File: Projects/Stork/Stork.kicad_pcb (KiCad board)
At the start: 4 copper layers, 200 x 100 mm, 567 parts, among them J1 Conn_01x05, J10 Conn_01x05, J11 Conn_01x05, J12 Conn_01x05, J13 Conn_01x05, J14 Conn_01x05, J15 Conn_01x05, J16 Conn_01x05, J17 Conn_01x05, J18 Conn_01x05, J19 Conn_01x05, J2 Conn_01x05, J20 Conn_01x05, J21 Conn_01x05, J22 Conn_01x05, J23 Conn_01x05, J24 Conn_01x05, J25 Conn_02x03_Odd_Even, J26 Conn_01x03_Male, J27 Screw_Terminal_01x02, J28 Conn_01x03_Male, J29 Conn_01x03_Male, J3 Conn_01x05, J30 Conn_01x03_Male, J4 Conn_01x05, J5 Conn_01x05, J6 Conn_01x05, J7 Conn_01x05, J8 Conn_01x05, J9 Conn_01x05, U1 AD7991YRJZ-1500RL7, U10 AD8608ARZ-SOIC127P600X175-14N, U11 AD7991YRJZ-1500RL7, U12 AD8608ARZ-SOIC127P600X175-14N, U13 AD7991YRJZ-1500RL7, U14 AD8608ARZ-SOIC127P600X175-14N, U15 AD7991YRJZ-1500RL7, U16 AD8608ARZ-SOIC127P600X175-14N, U17 AD7991YRJZ-1500RL7, U18 AD8608ARZ-SOIC127P600X175-14N, U19 AD7991YRJZ-1500RL7, U2 AD8608ARZ-SOIC127P600X175-14N, U20 AD8608ARZ-SOIC127P600X175-14N, U21 AD7991YRJZ-1500RL7, U22 AD8608ARZ-SOIC127P600X175-14N, U23 AD7991YRJZ-1500RL7, U24 AD8608ARZ-SOIC127P600X175-14N, U25 AD7991YRJZ-1500RL7, U26 AD8608ARZ-SOIC127P600X175-14N, U27 AD7991YRJZ-1500RL7, U28 AD8608ARZ-SOIC127P600X175-14N, U29 AD7991YRJZ-1500RL7, U3 AD7991YRJZ-1500RL7, U30 AD8608ARZ-SOIC127P600X175-14N, U31 AD7991YRJZ-1500RL7, U32 AD8608ARZ-SOIC127P600X175-14N, U33 Digilent-CoraZ7, U34 AD7991YRJZ-1500RL7, U35 AD8608ARZ-SOIC127P600X175-14N, U36 AD7991YRJZ-1500RL7, U37 AD8608ARZ-SOIC127P600X175-14N, U38 AD7991YRJZ-1500RL7, U39 AD8608ARZ-SOIC127P600X175-14N, U4 AD8608ARZ-SOIC127P600X175-14N, U40 AD7991YRJZ-1500RL7, U41 AD8608ARZ-SOIC127P600X175-14N, U42 AD7991YRJZ-1500RL7, U43 AD8608ARZ-SOIC127P600X175-14N, U44 AD7991YRJZ-1500RL7, U45 AD8608ARZ-SOIC127P600X175-14N, U46 AD7991YRJZ-1500RL7, U47 AD8608ARZ-SOIC127P600X175-14N, U48 AD7991YRJZ-1500RL7, U49 AD8608ARZ-SOIC127P600X175-14N, U5 AD7991YRJZ-1500RL7, U50 TPS79330-EP, U51 TPS73150DBV, U6 AD8608ARZ-SOIC127P600X175-14N, U7 AD7991YRJZ-1500RL7, U8 AD8608ARZ-SOIC127P600X175-14N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

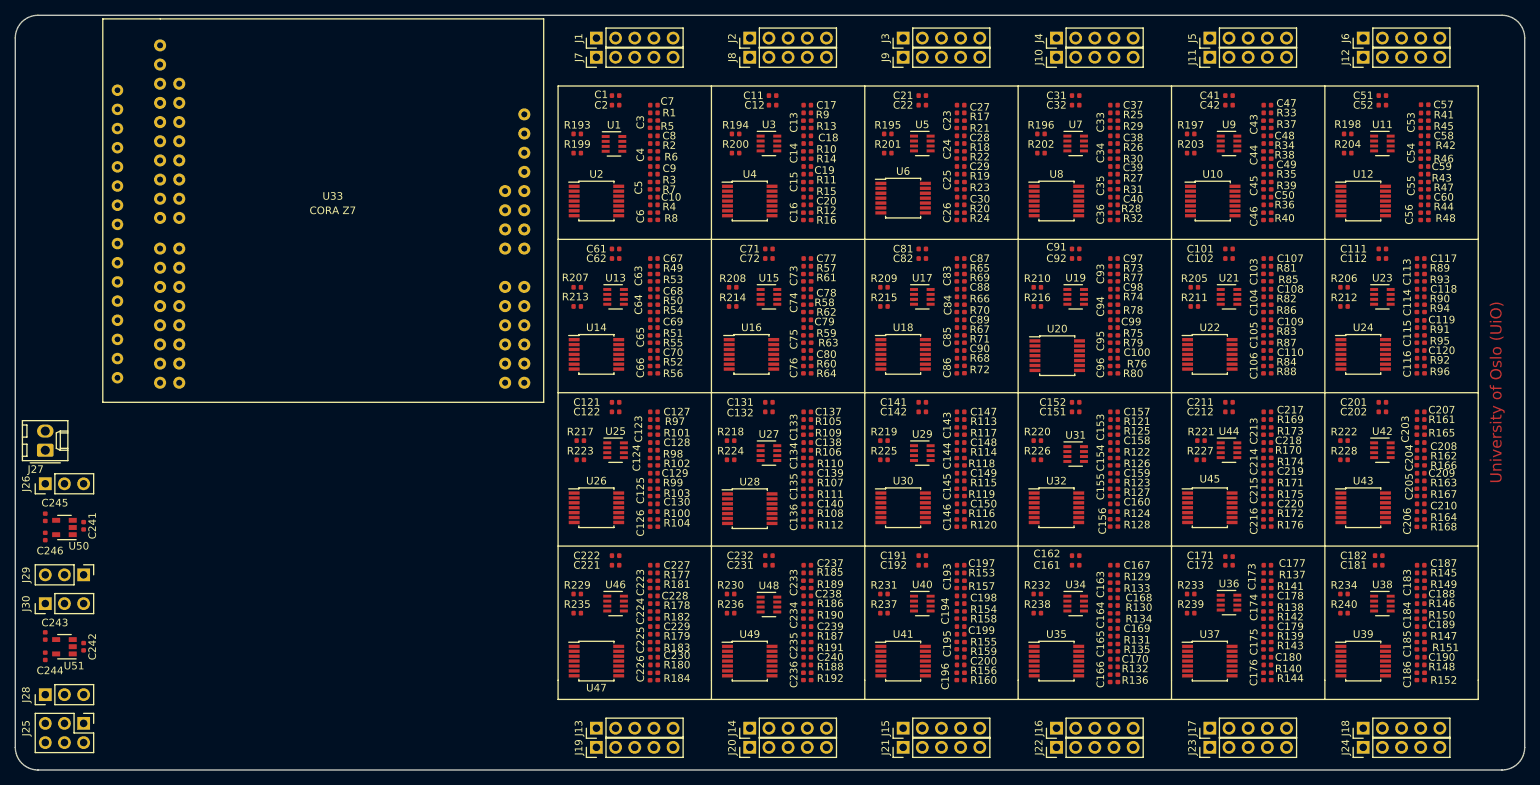
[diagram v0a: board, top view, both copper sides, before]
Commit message: replaced position of decoupling capacitors
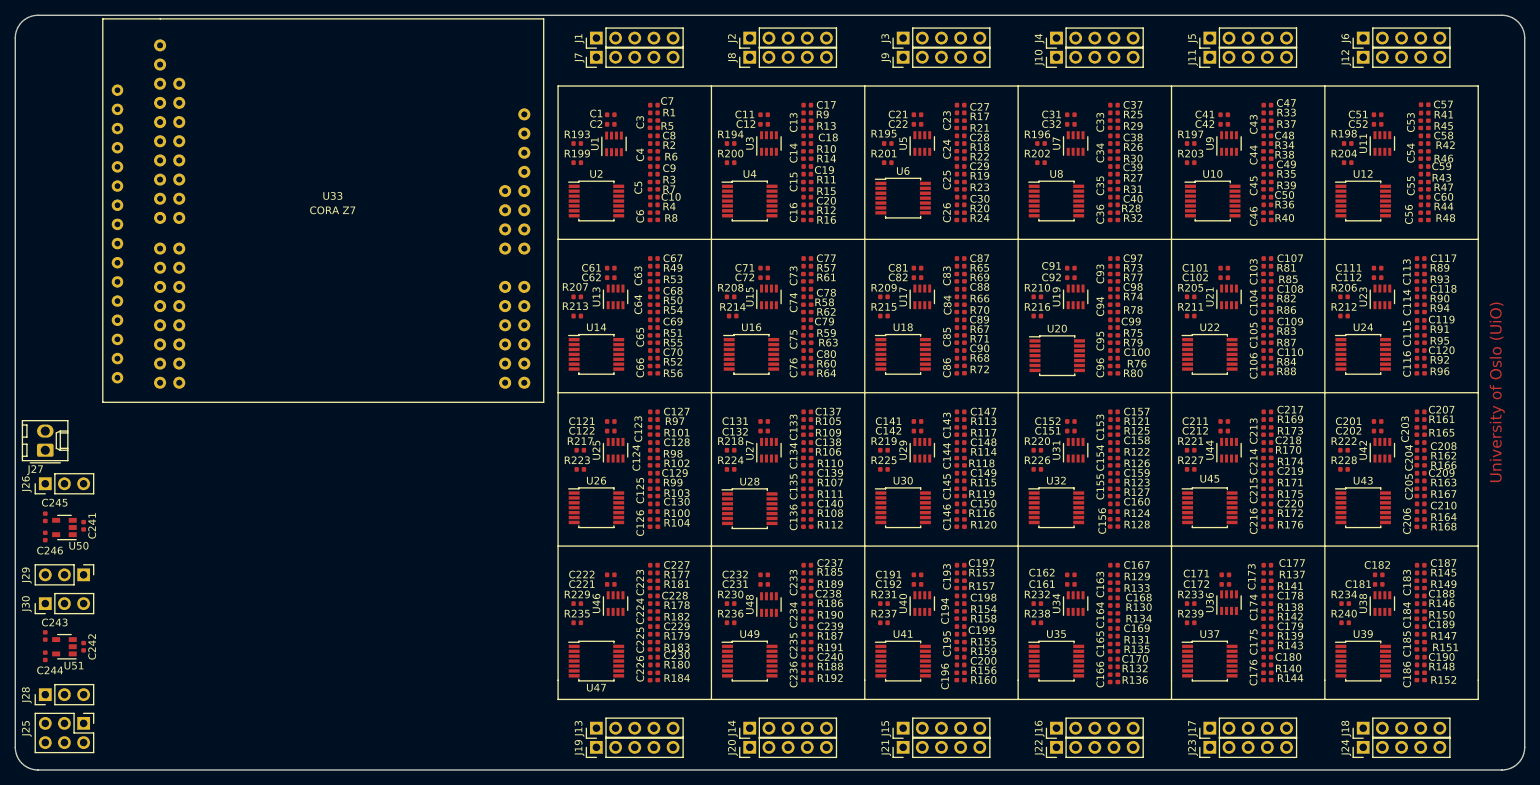
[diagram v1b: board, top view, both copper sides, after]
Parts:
- moved C12 2.78 mm to (149.2, 44.5)
- moved C11 2.78 mm to (149.2, 43.2)
- moved C132 2.62 mm to (149.2, 85.1)
- moved C142 2.62 mm to (169.5, 85.1)
- moved C191 2.62 mm to (169.5, 104.1)
- moved C22 2.62 mm to (169.5, 44.5)
- moved C232 2.62 mm to (149.2, 104.1)
- moved C122 2.62 mm to (128.9, 85.1)
- moved C151 2.62 mm to (189.9, 85.1)
- moved C162 2.62 mm to (189.9, 104.1)
- moved C2 2.62 mm to (128.9, 44.5)
- moved C202 2.62 mm to (230.5, 85.1)
- moved C212 2.62 mm to (210.2, 85.1)
- moved C222 2.62 mm to (128.9, 104.1)
- moved C32 2.62 mm to (189.9, 44.5)
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
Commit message: added vias for direct connection to ground and 3.3V plane. Done routing for power section
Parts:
- moved U10 0.38 mm to (208.3, 54.6)
- moved R214 0.28 mm to (144.8, 69.8)
- moved U6 0.25 mm to (167.6, 54.0)
- moved U16 0.22 mm to (147.3, 74.9)
- moved U20 0.17 mm to (188.1, 74.9)
- moved U28 0.13 mm to (147.3, 95.2)
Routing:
- net VDD_Filters: track 0.00 -> 662.7 mm, vias 0 -> 24
- net 5V_CoraZ7: track 0.00 -> 184.3 mm
- net V_RAW: track 0.00 -> 31.4 mm
- net 3V3_CoraZ7: track 0.00 -> 29.1 mm
- net +3V3: track 0.00 -> 28.5 mm, vias 0 -> 118
- net Net-(C241-Pad1): track 0.00 -> 10.9 mm
- net Net-(C242-Pad1): track 0.00 -> 10.6 mm
- net GND: track 0.35 -> 10.4 mm, vias 0 -> 172
- net 5V_Reg: track 0.00 -> 9.47 mm
- net 3V3_Reg: track 0.00 -> 6.34 mm
- net +5V: track 0.00 -> 4.86 mm
- net Net-(C243-Pad1): track 0.00 -> 2.32 mm
- net Net-(C245-Pad1): track 0.00 -> 1.81 mm
- added copper zone on In2.Cu, net +3V3
- added copper zone on In1.Cu, net GND

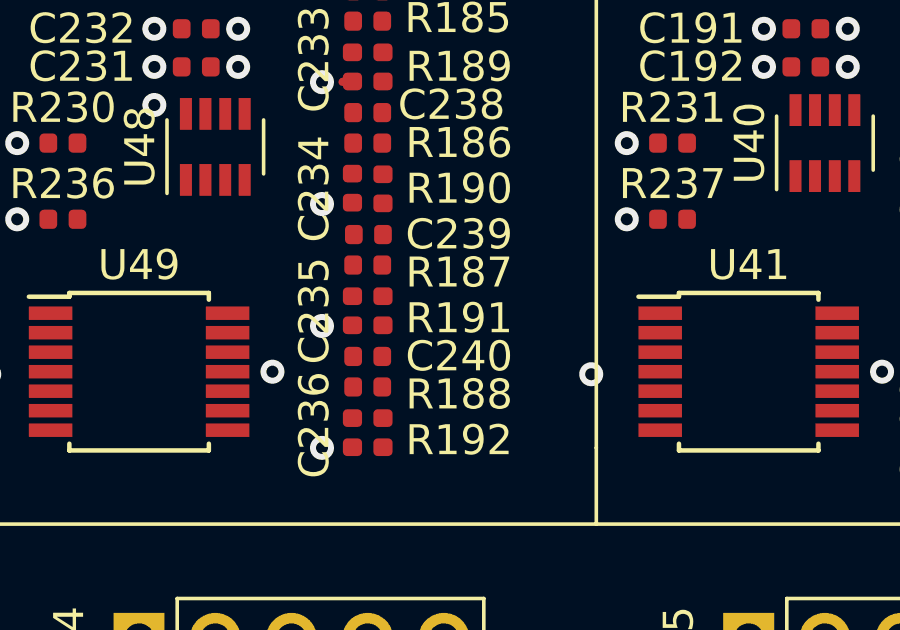
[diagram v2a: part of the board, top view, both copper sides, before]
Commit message: R191 rotated
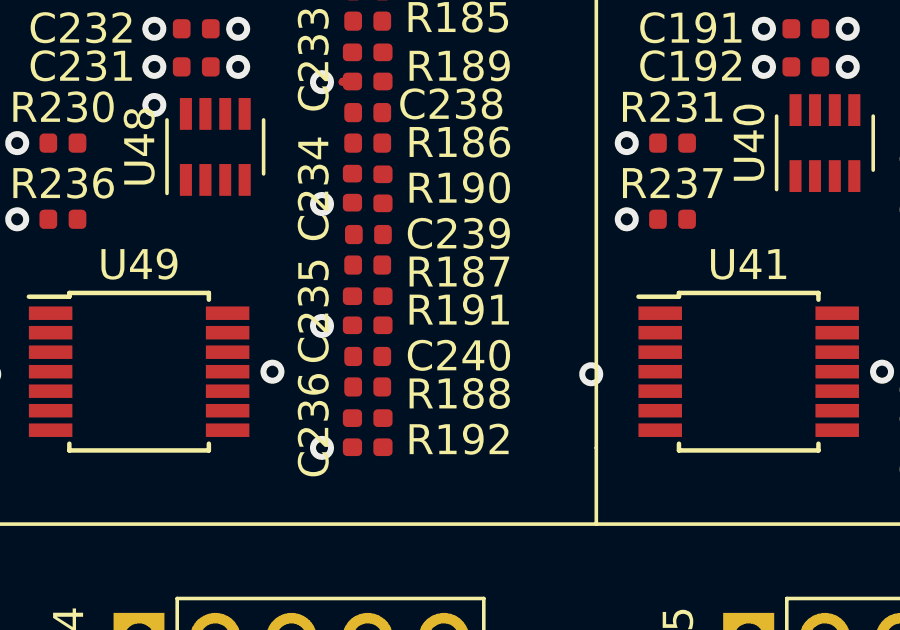
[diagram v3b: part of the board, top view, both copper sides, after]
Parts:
- turned R191 to 90 degrees
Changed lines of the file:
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@@
   )
   (setup
-    (last_trace_width 0.5)
+    (last_trace_width 0.25)
     (user_trace_width 0.5)
     (user_trace_width 1)
@@
   )
   (module Resistor_SMD:R_0402_1005Metric (layer F.Cu)
-    (at 155.448 113.538 270)
+    (at 155.448 113.538 90)
     (descr "Resistor SMD 0402 (1005 Metric), square (rectangular) end terminal, IPC_7351 nominal, (Body size source: http://www.tortai-tech.com/upload/download/2011102023233369053.pdf), generated with kicad-footprint-generator")
     (tags resistor)
     (attr smd)
-    (fp_text reference R191 (at 0.254 -2.54 180) (layer F.SilkS)
+    (fp_text reference R191 (at 0 2.54 180) (layer F.SilkS)
       (effects (font (size 1 1) (thickness 0.15)))
     )
@@
     (fp_line (start -0.5 -0.25) (end 0.5 -0.25) (layer F.Fab) (width 0.1))
     (fp_line (start -0.5 0.25) (end -0.5 -0.25) (layer F.Fab) (width 0.1))
-    (pad 2 smd roundrect (at 0.485 0 270) (size 0.59 0.64) (layers F.Cu F.Paste F.Mask) (roundrect_rratio 0.25)
+    (pad 2 smd roundrect (at 0.485 0 90) (size 0.59 0.64) (layers F.Cu F.Paste F.Mask) (roundrect_rratio 0.25)
       (net 286 "Net-(C239-Pad2)"))
-    (pad 1 smd roundrect (at -0.485 0 270) (size 0.59 0.64) (layers F.Cu F.Paste F.Mask) (roundrect_rratio 0.25)
+    (pad 1 smd roundrect (at -0.485 0 90) (size 0.59 0.64) (layers F.Cu F.Paste F.Mask) (roundrect_rratio 0.25)
       (net 380 VIN2_19))
     (model ${KISYS3DMOD}/Resistor_SMD.3dshapes/R_0402_1005Metric.wrl
@@
   (segment (start 59.055 114.935) (end 59.182 115.062) (width 0.5) (layer F.Cu) (net 1))
   (segment (start 59.055 114.15) (end 59.055 114.935) (width 0.5) (layer F.Cu) (net 1))
-  (via (at 122.936 49.53) (size 0.8) (drill 0.4) (layers F.Cu B.Cu) (net 447))
-  (via (at 122.936 46.99) (size 0.8) (drill 0.4) (layers F.Cu B.Cu) (net 447))
   (segment (start 134.112 104.925) (end 133.792 104.925) (width 0.25) (layer F.Cu) (net 266))
   (segment (start 134.135 104.902) (end 134.112 104.925) (width 0.25) (layer F.Cu) (net 266))
@@
   (segment (start 59.055 123.317) (end 59.055 123.825) (width 1) (layer In2.Cu) (net 394))
   (segment (start 56.515 120.777) (end 59.055 123.317) (width 1) (layer In2.Cu) (net 394))
+  (via (at 122.936 49.53) (size 0.8) (drill 0.4) (layers F.Cu B.Cu) (net 447))
+  (via (at 122.936 46.99) (size 0.8) (drill 0.4) (layers F.Cu B.Cu) (net 447))
   (via (at 143.256 46.99) (size 0.8) (drill 0.4) (layers F.Cu B.Cu) (net 447))
   (via (at 143.256 49.53) (size 0.8) (drill 0.4) (layers F.Cu B.Cu) (net 447))
